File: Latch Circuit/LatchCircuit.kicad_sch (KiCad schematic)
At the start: 22 parts, among them J1 Screw_Terminal_01x10, J2 Screw_Terminal_01x01, J3 Screw_Terminal_01x02, U1 40106, U2 4013, U3 4013, U4 4013, U5 4002, U6 40106, U7 40106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

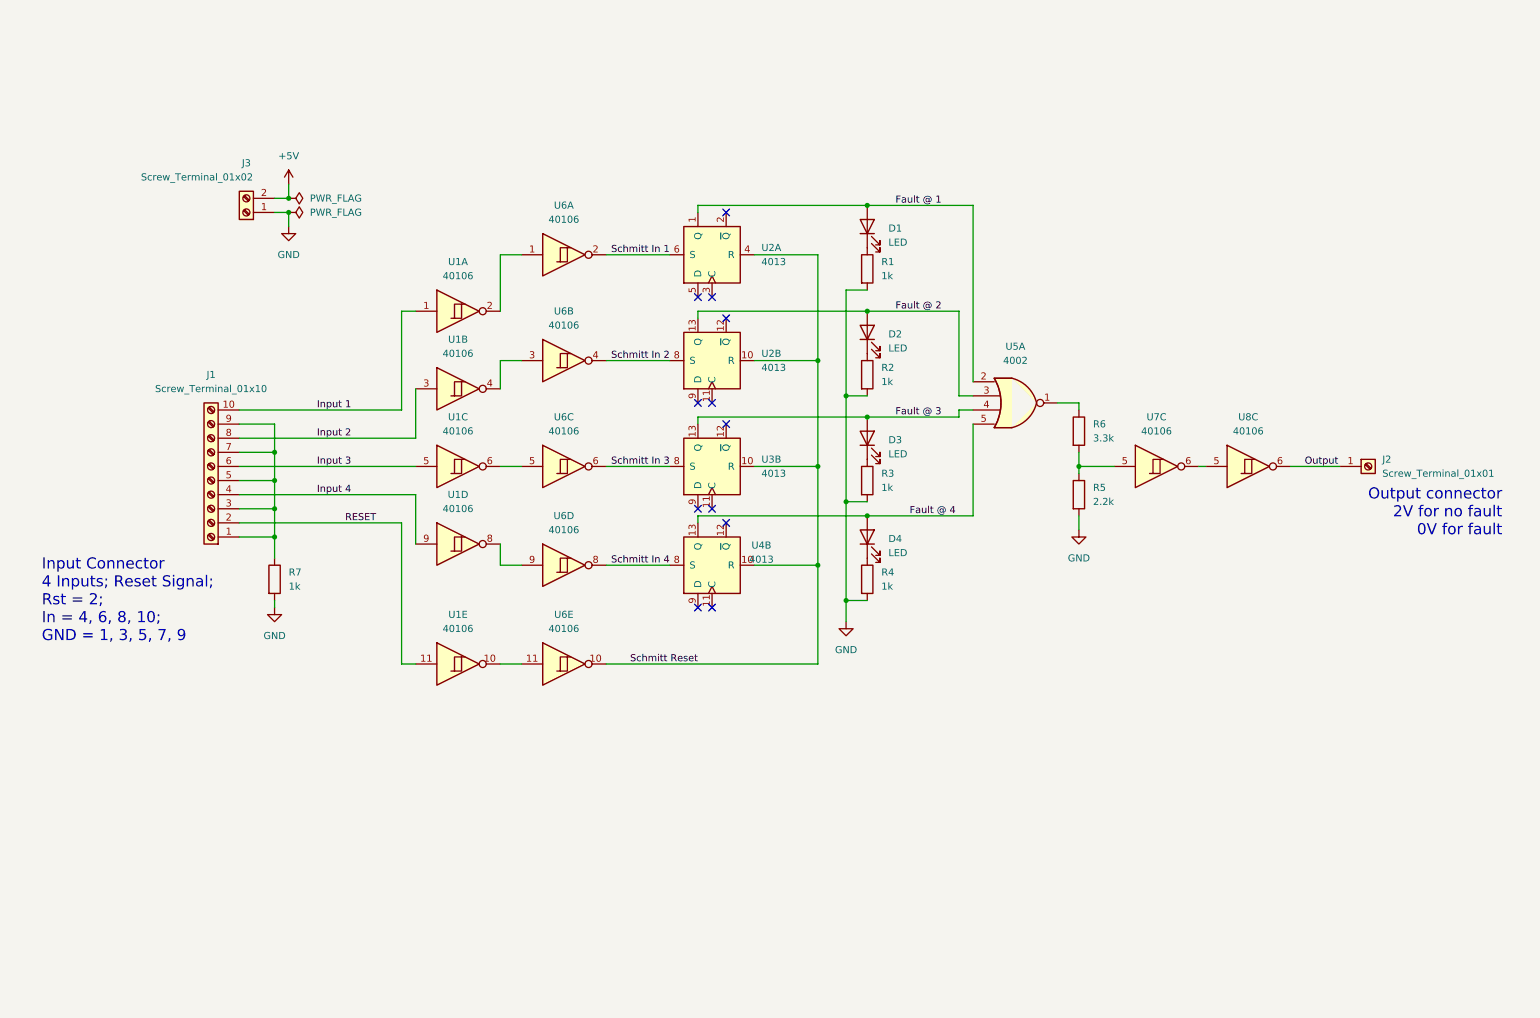
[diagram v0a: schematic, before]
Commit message: update circuitry to include relays; change from screw terminals to connectors
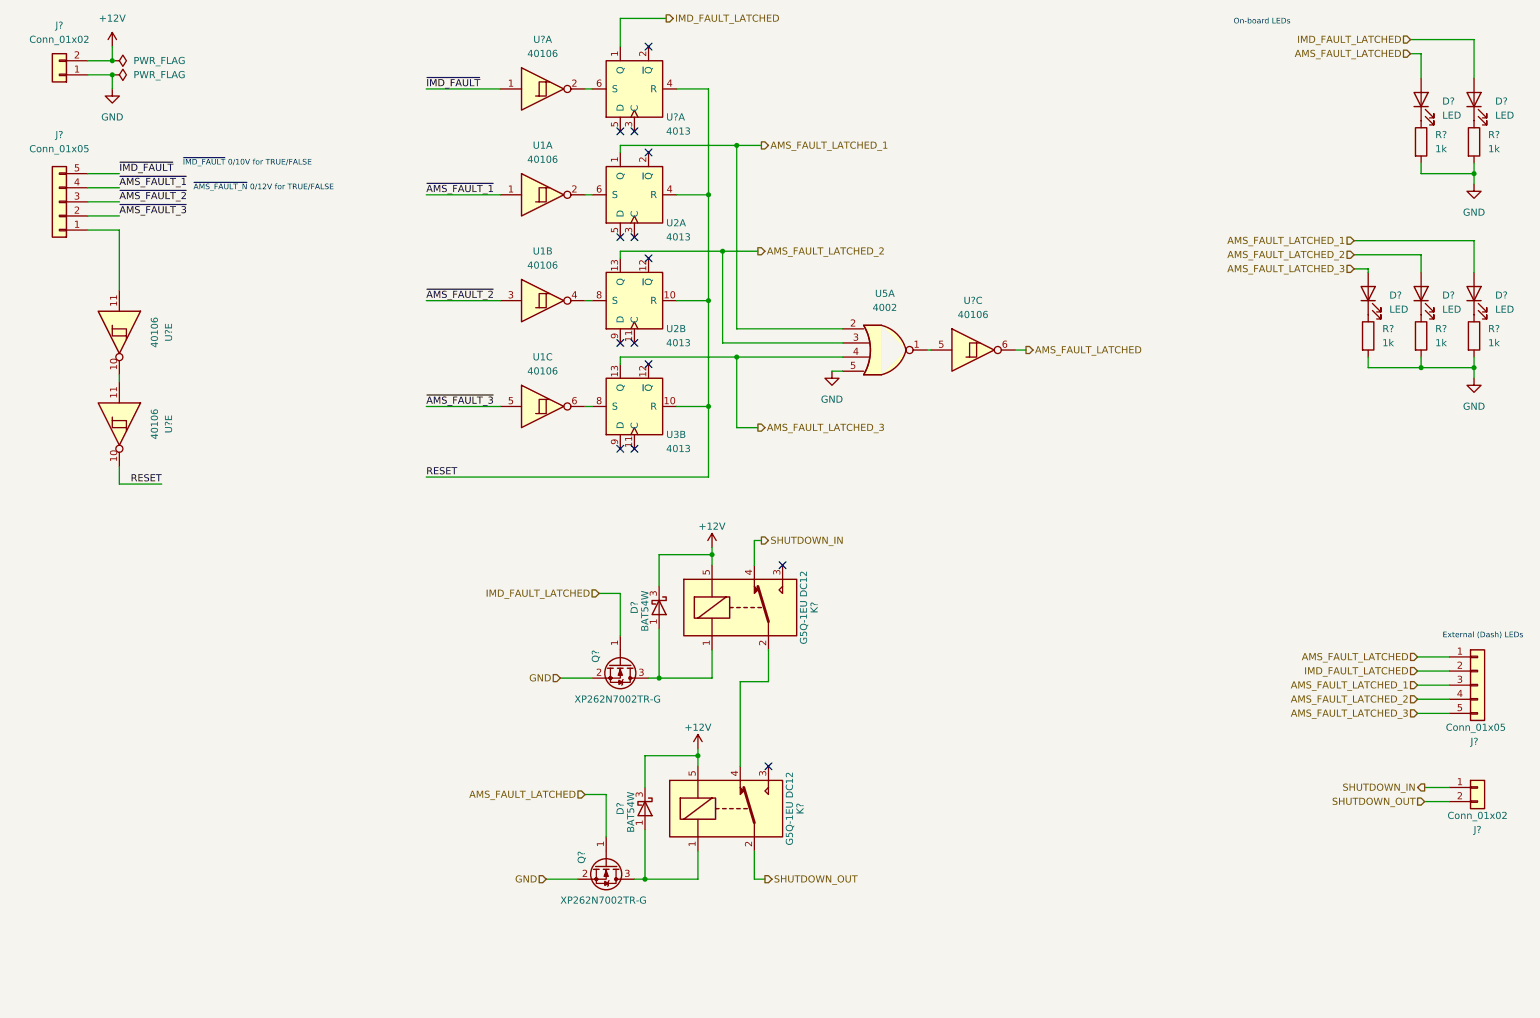
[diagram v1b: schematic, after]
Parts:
- removed D1, D2, D3, D4: LED, LED_THT:LED_D5.0mm, symbol Device:LED
- removed J1: Screw_Terminal_01x10, Connector_PinHeader_1.27mm:PinHeader_1x10_P1.27mm_Vertical, symbol Connector:Screw_Terminal_01x10
- removed J2: Screw_Terminal_01x01, Connector_PinHeader_1.27mm:PinHeader_1x01_P1.27mm_Vertical, symbol Connector:Screw_Terminal_01x01
- removed J3: Screw_Terminal_01x02, Connector_PinHeader_1.27mm:PinHeader_1x02_P1.27mm_Vertical, symbol Connector:Screw_Terminal_01x02
- removed R1, R2, R3, R4, R7: 1k, Resistor_THT:R_Axial_DIN0309_L9.0mm_D3.2mm_P15.24mm_Horizontal, symbol Device:R
- removed R5: 2.2k, Resistor_THT:R_Axial_DIN0309_L9.0mm_D3.2mm_P15.24mm_Horizontal, symbol Device:R
- removed R6: 3.3k, Resistor_THT:R_Axial_DIN0309_L9.0mm_D3.2mm_P15.24mm_Horizontal, symbol Device:R
- removed unit 5 of U1
- removed unit 4 of U1
- removed U4: 4013, symbol 4xxx:4013
- removed U6, U7, U8: 40106, symbol 4xxx:40106
- added D? (x5): LED, LED_THT:LED_D5.0mm, symbol Device:LED
- added D? (x2): BAT54W, Package_TO_SOT_SMD:SOT-323_SC-70, symbol Diode:BAT54W
- added J? (x2): Conn_01x02, Connector_Molex:Molex_Micro-Fit_3.0_43650-0200_1x02_P3.00mm_Horizontal, symbol Connector_Generic:Conn_01x02
- added J? (x2): Conn_01x05, symbol Connector_Generic:Conn_01x05
- added K? (x2): G5Q-1EU DC12, Relay_THT:Relay_SPDT_Omron-G5Q-1, symbol Relay:G5Q-1
- added Q? (x2): XP262N7002TR-G, Package_TO_SOT_SMD:SOT-23, symbol Device:Q_NMOS_GSD
- added R? (x5): 1k, Resistor_THT:R_Axial_DIN0309_L9.0mm_D3.2mm_P15.24mm_Horizontal, symbol Device:R
- added U? (x4): 40106, symbol 4xxx:40106
- added U?: 4013, symbol 4xxx:4013
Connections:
- net Fault @ 4 is gone; now on net GND: U5.5
- net Schmitt In 1 is gone; now on an unnamed net: U2.6 (S)
- net Schmitt In 2 is gone; now on an unnamed net: U2.8 (S)
- net Schmitt In 3 is gone; now on an unnamed net: U3.8 (S)
- net Schmitt Reset is gone; now on net RESET: U2.10 (R), U2.4 (R), U3.10 (R)
- net GND: now also J?.1 (Pin_1), Q?.2 (S), Q?.2 (S), R?.2, R?.2, R?.2, R?.2, R?.2
- net RESET: now also U?.10, U?.4 (R)
- net at U5.1: now also U?.5
- net Fault @ 1 renamed AMS_FAULT_LATCHED_1
- net AMS_FAULT_LATCHED_1: now also D?.2 (A), J?.3 (Pin_3)
- net Fault @ 2 renamed AMS_FAULT_LATCHED_2
- net AMS_FAULT_LATCHED_2: now also D?.2 (A), J?.4 (Pin_4)
- net Fault @ 3 renamed AMS_FAULT_LATCHED_3
- net AMS_FAULT_LATCHED_3: now also D?.2 (A), J?.5 (Pin_5)
- net Input 1 renamed ~{AMS_FAULT_1}
- net ~{AMS_FAULT_1}: now also J?.4 (Pin_4)
- net Input 2 renamed ~{AMS_FAULT_2}
- net ~{AMS_FAULT_2}: now also J?.3 (Pin_3)
- net Input 3 renamed ~{AMS_FAULT_3}
- net ~{AMS_FAULT_3}: now also J?.2 (Pin_2)
- new net: D?.1 (K), R?.1 (x5)
- new net: D?.1 (A), K?.1, Q?.3 (D) (x2)
- new net: K?.2, K?.4
- new net: J?.1 (Pin_1), U?.11
- new net: U?.10, U?.11
- new net: U?.2, U?.6 (S)
- new net +12V: D?.3 (K), D?.3 (K), J?.2 (Pin_2), K?.5, K?.5
- new net AMS_FAULT_LATCHED: D?.2 (A), J?.1 (Pin_1), Q?.1 (G), U?.6
- new net IMD_FAULT_LATCHED: D?.2 (A), J?.2 (Pin_2), Q?.1 (G), U?.1 (Q)
- new net SHUTDOWN_IN: J?.1 (Pin_1), K?.4
- new net SHUTDOWN_OUT: J?.2 (Pin_2), K?.2
- new net ~{IMD_FAULT}: J?.5 (Pin_5), U?.1
- no-connect marks 12 -> 14
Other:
- note added: "External (Dash) LEDs"
- note added: "On-board LEDs"
- note added: "~{AMS_FAULT_N} 0/12V for TRUE/FALSE"
- note added: "~{IMD_FAULT} 0/10V for TRUE/FALSE"
- note removed: "Input Connector 4 Inputs; Reset Signal; Rst = 2; In = 4, 6, 8, 10; GND = 1, 3, 5, 7, 9"
- note removed: "Output connector 2V for no fault 0V for fault"
- moved on the sheet: U1A, U1B, U1C, U2A, U2B, U3B, U5A

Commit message: separate latching to sheet; create windowing sheet; minor cleanup/refactoring
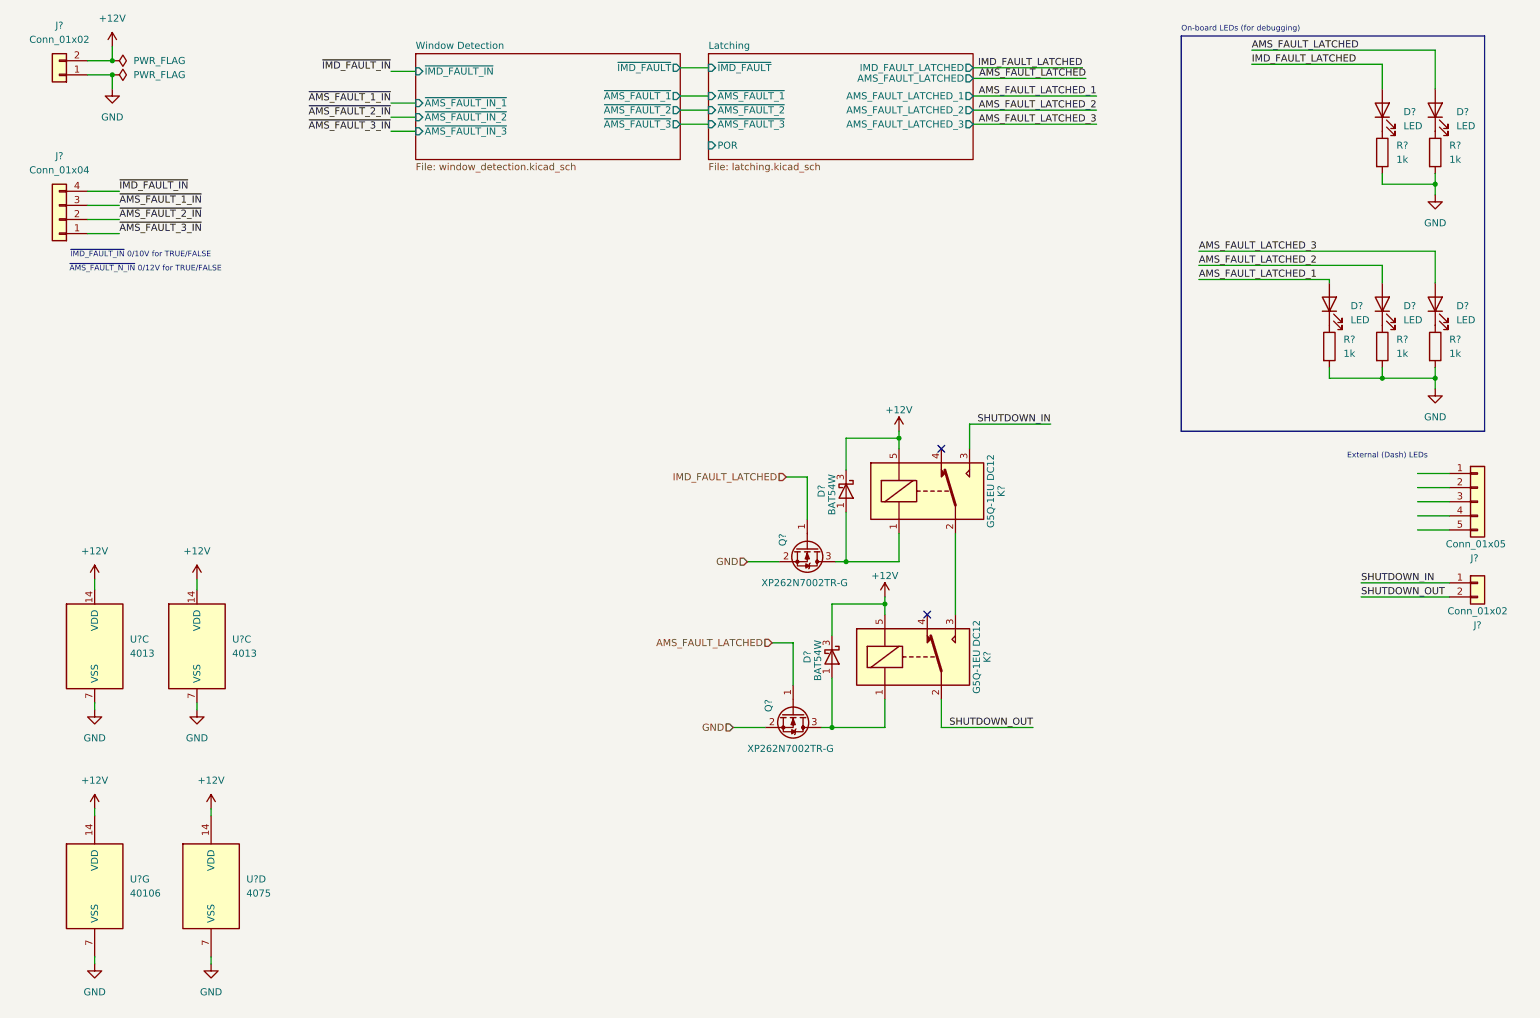
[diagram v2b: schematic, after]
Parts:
- removed J?: Conn_01x05, symbol Connector_Generic:Conn_01x05
- removed U1, U? (x4): 40106, symbol 4xxx:40106
- removed U2, U3, U?: 4013, symbol 4xxx:4013
- removed U5: 4002, symbol 4xxx:4002
- added J?: Conn_01x04, symbol Connector_Generic:Conn_01x04
- added U?: 40106, symbol 4xxx:40106
- added U?: 4075, symbol 4xxx:4075
- added U? (x2): 4013, symbol 4xxx:4013
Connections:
- net +12V: now also U?.14 (VDD), U?.14 (VDD), U?.14 (VDD), U?.14 (VDD)
- net AMS_FAULT_LATCHED: now also D?.2 (A); no longer D?.2 (A), J?.1 (Pin_1)
- net AMS_FAULT_LATCHED_1: now also D?.2 (A); no longer D?.2 (A), J?.3 (Pin_3)
- net AMS_FAULT_LATCHED_2: no longer J?.4 (Pin_4)
- net AMS_FAULT_LATCHED_3: now also D?.2 (A); no longer D?.2 (A), J?.5 (Pin_5)
- net GND: now also U?.7 (VSS), U?.7 (VSS), U?.7 (VSS), U?.7 (VSS)
- net IMD_FAULT_LATCHED: now also D?.2 (A); no longer D?.2 (A), J?.2 (Pin_2)
- net SHUTDOWN_IN: now also K?.3; no longer K?.4
- net at K?.2: now also K?.3; no longer K?.4
- new net ~{AMS_FAULT_1_IN}: J?.3 (Pin_3)
- new net ~{AMS_FAULT_2_IN}: J?.2 (Pin_2)
- new net ~{AMS_FAULT_3_IN}: J?.1 (Pin_1)
- new net ~{IMD_FAULT_IN}: J?.4 (Pin_4)
- no-connect marks 14 -> 2
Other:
- added sheet Latching (latching.kicad_sch)
- added sheet Window Detection (window_detection.kicad_sch)
- note added: "On-board LEDs (for debugging)"
- note added: "~{AMS_FAULT_N_IN} 0/12V for TRUE/FALSE"
- note added: "~{IMD_FAULT_IN} 0/10V for TRUE/FALSE"
- note removed: "On-board LEDs"
- note removed: "~{AMS_FAULT_N} 0/12V for TRUE/FALSE"
- note removed: "~{IMD_FAULT} 0/10V for TRUE/FALSE"
- moved on the sheet: D?, J?, K?, Q?, R?

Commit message: (wip) update OK condition inputs from IMD, AMS
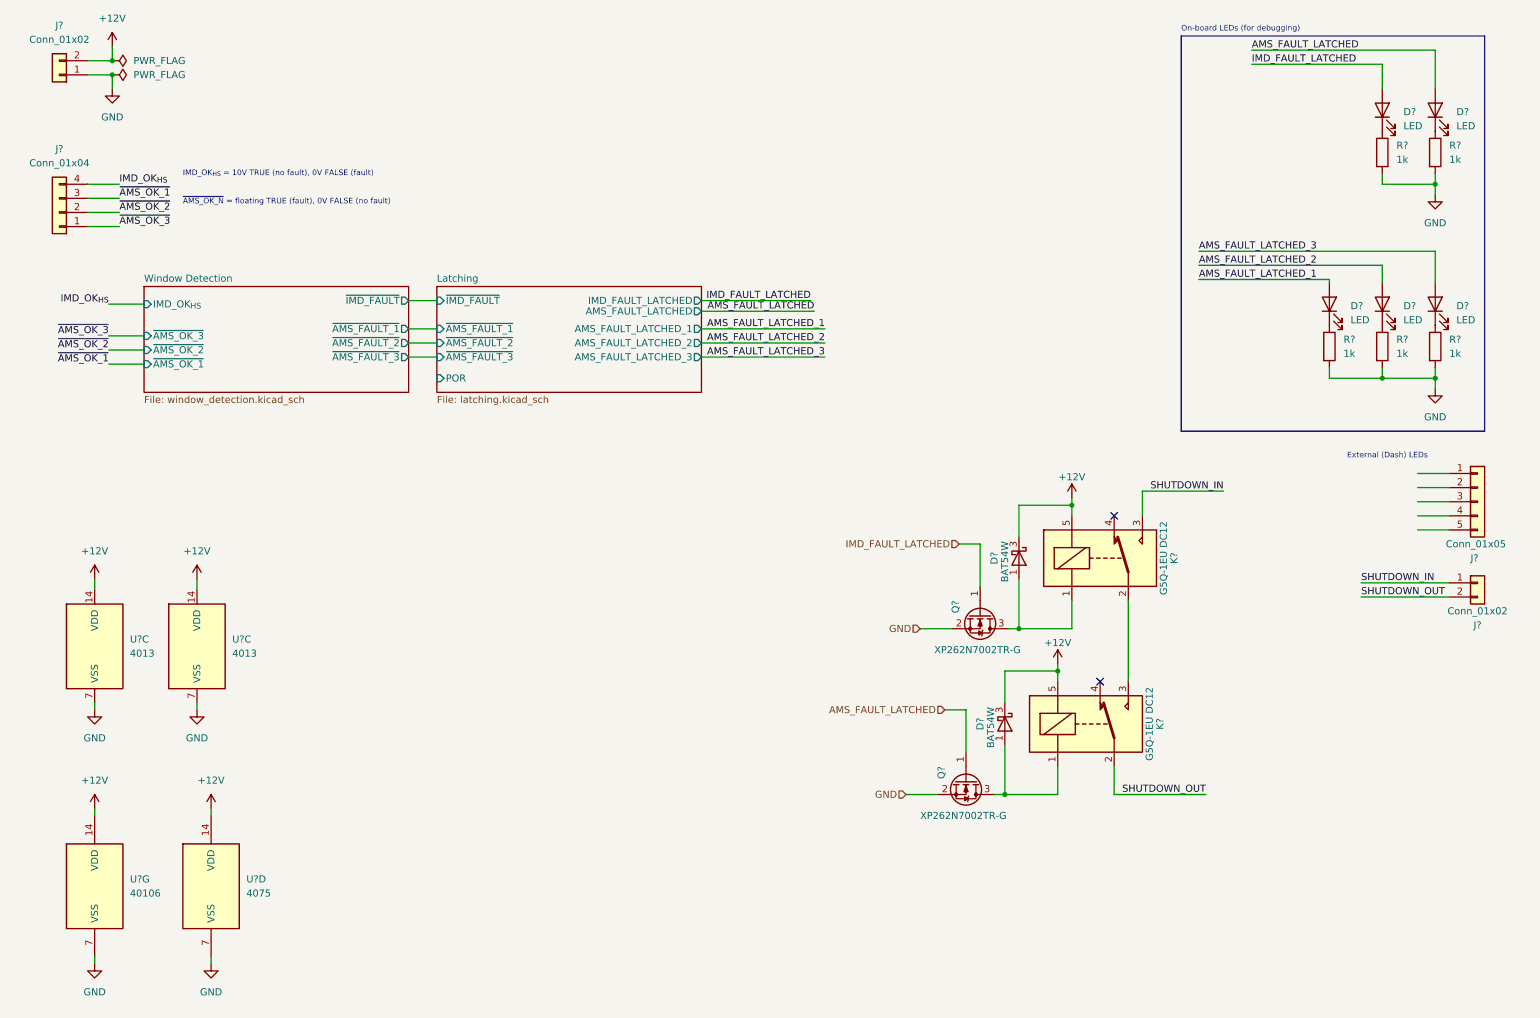
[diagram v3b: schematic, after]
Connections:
- net ~{AMS_FAULT_1_IN} renamed ~{AMS_OK_1}
- net ~{AMS_FAULT_2_IN} renamed ~{AMS_OK_2}
- net ~{AMS_FAULT_3_IN} renamed ~{AMS_OK_3}
- net ~{IMD_FAULT_IN} renamed IMD_OK_{HS}
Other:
- sheet Window Detection ports: added IMD_OK_{HS}, ~{AMS_OK_1}, ~{AMS_OK_2}, ~{AMS_OK_3}; removed ~{AMS_FAULT_IN_1}, ~{AMS_FAULT_IN_2}, ~{AMS_FAULT_IN_3}, ~{IMD_FAULT_IN}
- note added: "IMD_OK_{HS} = 10V TRUE (no fault), 0V FALSE (fault)"
- note added: "~{AMS_OK_N} = floating TRUE (fault), 0V FALSE (no fault)"
- note removed: "~{AMS_FAULT_N_IN} 0/12V for TRUE/FALSE"
- note removed: "~{IMD_FAULT_IN} 0/10V for TRUE/FALSE"
- moved on the sheet: D?, J?, K?, Q?
